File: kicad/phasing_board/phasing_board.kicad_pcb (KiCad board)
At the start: 4 copper layers, 103.2 x 30 mm, 4 parts, among them J1 EdgeLaunch_SMA_BNC_F_1.6mm, P1 PhasingTab_TAB1, P2 PhasingTab_TAB2

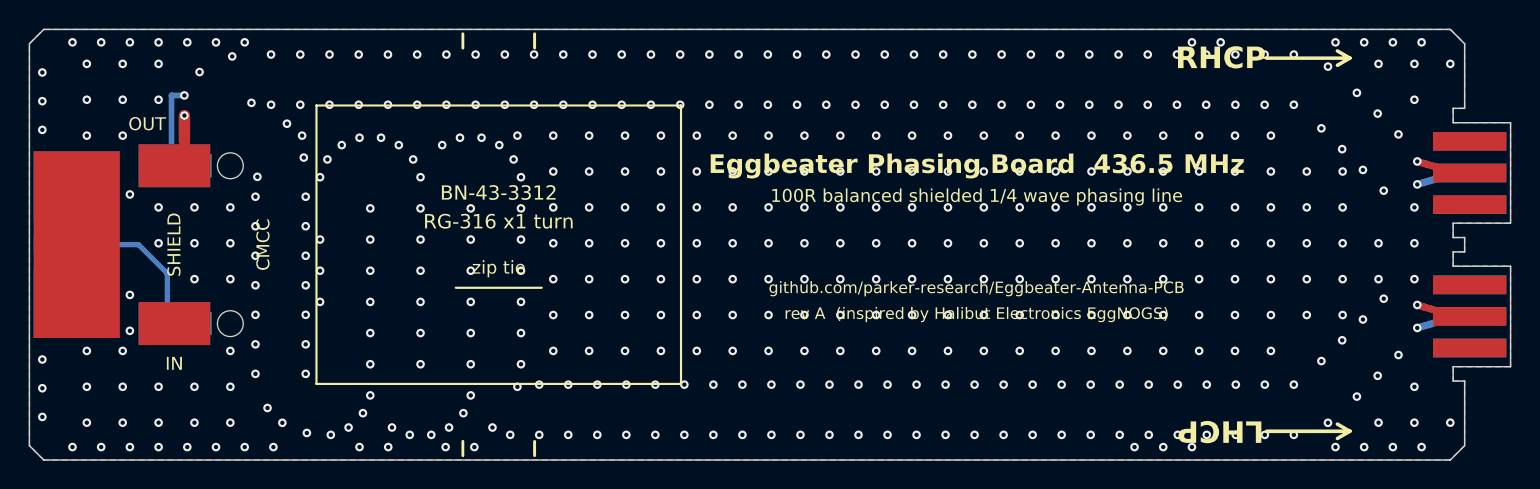
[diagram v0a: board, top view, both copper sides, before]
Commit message: HACK: Shrink PCB under 100mm long to check pricing
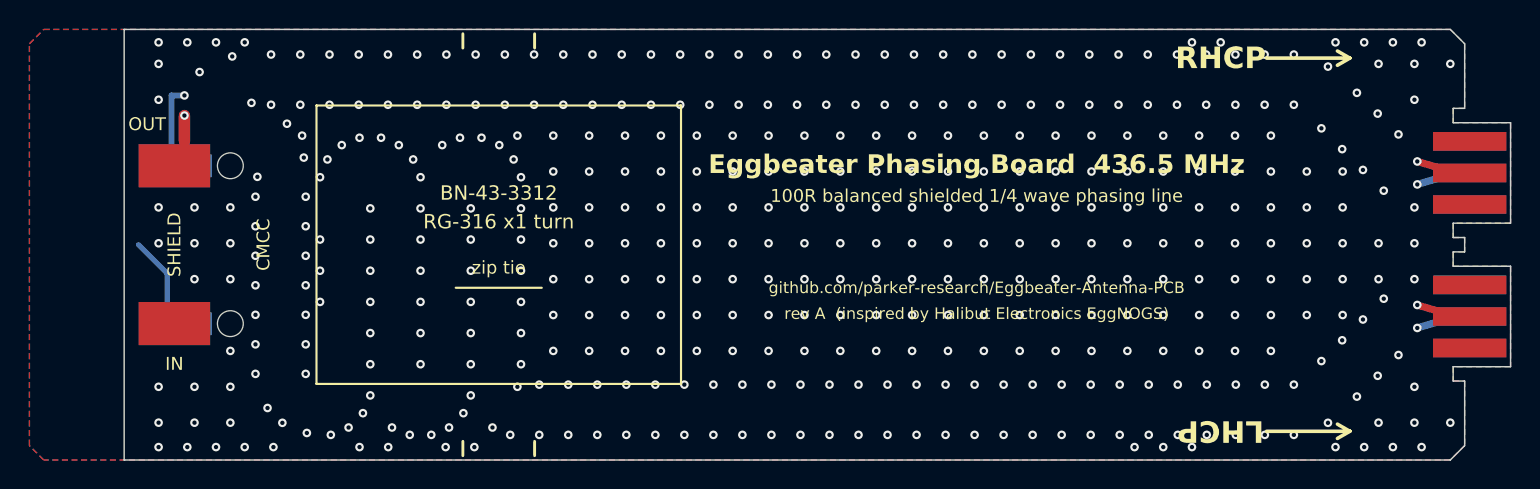
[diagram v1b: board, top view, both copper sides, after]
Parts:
- removed J1: EdgeLaunch_SMA_BNC_F_1.6mm, EggbeaterAntenna:EdgeLaunch_SMA_BNC_F_1.6mm
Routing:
- net RF_IN: track 8.93 -> 6.73 mm
- net GND: vias 461 -> 434
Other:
- board size 103.2 x 30 mm -> 96.6 x 30 mm
